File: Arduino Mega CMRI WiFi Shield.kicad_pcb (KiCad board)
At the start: 2 copper layers, 100 x 56 mm, 37 parts, among them IC2 VoltageRegulator-5V-3V3-TH, J1 Socket-2x4-TH, J10 Header-1x4-TH, J11 Header-1x4-TH, J12 Header-1x4-TH, J13 Header-1x4-TH, J14 Header-1x4-TH, J15 Header-1x4-TH, J16 Header-1x4-TH, J17 Header-1x4-TH, J18 Header-1x3-TH, J2 Header-1x4-TH, J3 Header-1x4-TH, J4 Header-1x4-TH, J5 Header-1x4-TH, J6 Header-1x4-TH, J7 Header-1x4-TH, J8 Header-1x4-TH, J9 Header-1x4-TH, Q1 Transistor-FET-.2A-2.6V-TH, Q2 Transistor-FET-.2A-2.6V-TH, Q3 Transistor-FET-.2A-2.6V-TH

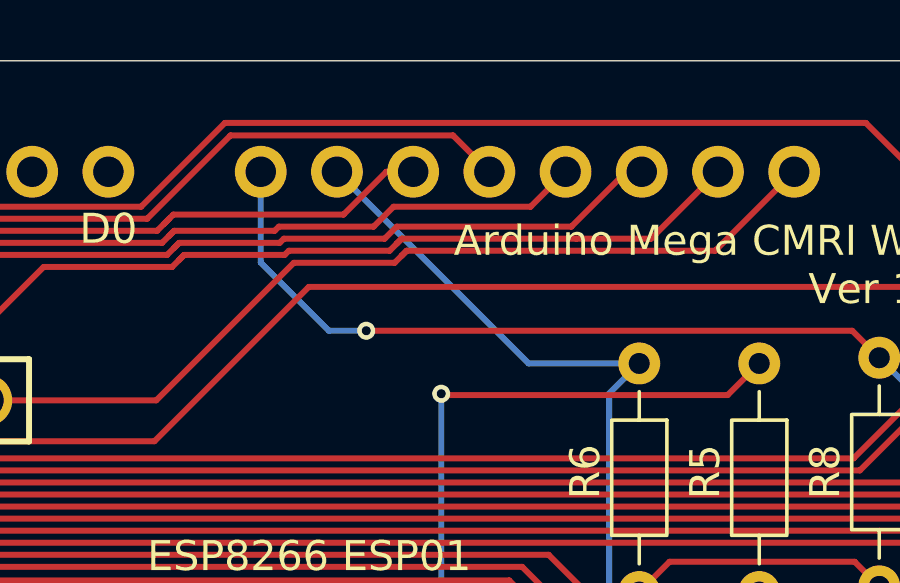
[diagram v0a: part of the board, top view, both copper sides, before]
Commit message: Swapped the RX and TX pins between the arduino and the ESP8266-ESP01 that was discovered on prototype board v1.2
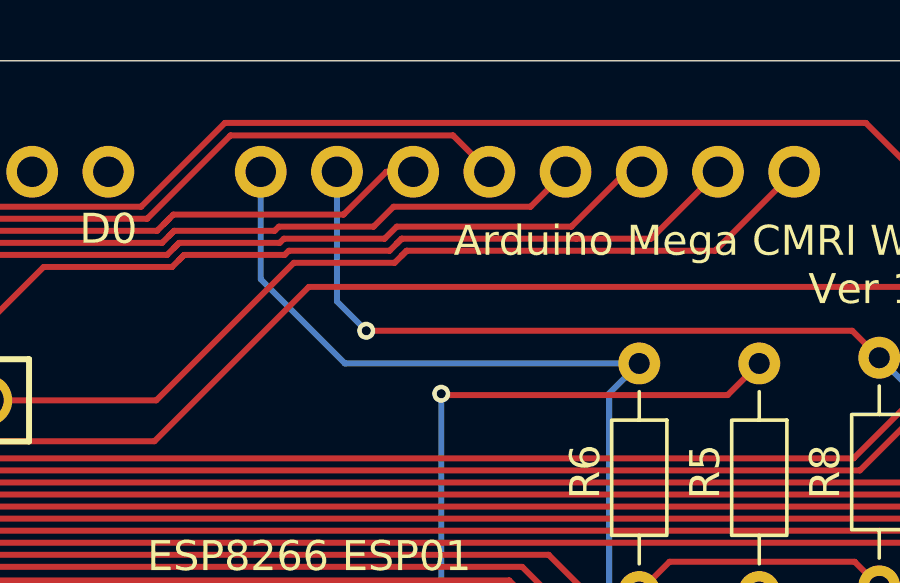
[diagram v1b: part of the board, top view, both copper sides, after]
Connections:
- A1 pad D14: /ESP8266ESP01WiFi/TX -> /ESP8266ESP01WiFi/RX
- A1 pad D15: /ESP8266ESP01WiFi/RX -> /ESP8266ESP01WiFi/TX
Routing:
- net /ESP8266ESP01WiFi/RX: track 39.2 -> 43.8 mm
- net /ESP8266ESP01WiFi/TX: track 50.8 -> 49.0 mm
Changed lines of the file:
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@@
 			)
 		)
-		(property "Datasheet" ""
+		(property "Datasheet" "https://www.mouser.com/datasheet/3/508/1/YAGEO_CFR_DATASHEET.pdf"
 			(at 0 0 270)
 			(layer "F.Fab")
@@
 			)
 		)
-		(property "Description" ""
+		(property "Description" "Resistor - 10K- 1/4W - 5% - Through Hole"
 			(at 0 0 270)
 			(layer "F.Fab")
@@
 			)
 		)
-		(property "Datasheet" ""
+		(property "Datasheet" "https://www.mouser.com/datasheet/3/508/1/YAGEO_CFR_DATASHEET.pdf"
 			(at 0 0 270)
 			(layer "F.Fab")
@@
 			)
 		)
-		(property "Description" ""
+		(property "Description" "Resistor - 10K- 1/4W - 5% - Through Hole"
 			(at 0 0 270)
 			(layer "F.Fab")
@@
 			(layers "*.Cu" "*.Mask")
 			(remove_unused_layers no)
-			(net 62 "/ESP8266ESP01WiFi/TX")
+			(net 71 "/ESP8266ESP01WiFi/RX")
 			(pinfunction "D14/TX3")
 			(pintype "bidirectional")
@@
 			(layers "*.Cu" "*.Mask")
 			(remove_unused_layers no)
-			(net 71 "/ESP8266ESP01WiFi/RX")
+			(net 62 "/ESP8266ESP01WiFi/TX")
 			(pinfunction "D15/RX3")
 			(pintype "bidirectional")
@@
 			)
 		)
-		(property "Datasheet" ""
+		(property "Datasheet" "https://www.mouser.com/datasheet/3/508/1/YAGEO_CFR_DATASHEET.pdf"
 			(at 0 0 270)
 			(layer "F.Fab")
@@
 			)
 		)
-		(property "Description" ""
+		(property "Description" "Resistor - 10K- 1/4W - 5% - Through Hole"
 			(at 0 0 270)
 			(layer "F.Fab")
@@
 			)
 		)
-		(property "Datasheet" ""
+		(property "Datasheet" "https://www.mouser.com/datasheet/3/508/1/YAGEO_CFR_DATASHEET.pdf"
 			(at 0 0 270)
 			(layer "F.Fab")
@@
 			)
 		)
-		(property "Description" ""
+		(property "Description" "Resistor - 10K- 1/4W - 5% - Through Hole"
 			(at 0 0 270)
 			(layer "F.Fab")
@@
 			)
 		)
-		(property "Datasheet" ""
+		(property "Datasheet" "https://www.mouser.com/datasheet/3/508/1/YAGEO_CFR_DATASHEET.pdf"
 			(at 0 0 270)
 			(layer "F.Fab")
@@
 			)
 		)
-		(property "Description" ""
+		(property "Description" "Resistor - 10K- 1/4W - 5% - Through Hole"
 			(at 0 0 270)
 			(layer "F.Fab")
@@
 			)
 		)
-		(property "Datasheet" ""
+		(property "Datasheet" "https://www.mouser.com/datasheet/3/508/1/YAGEO_CFR_DATASHEET.pdf"
 			(at 0 0 270)
 			(layer "F.Fab")
@@
 			)
 		)
-		(property "Description" ""
+		(property "Description" "Resistor - 10K- 1/4W - 5% - Through Hole"
 			(at 0 0 270)
 			(layer "F.Fab")
@@
 	)
 	(segment
-		(start 154.9 56.1)
-		(end 153.6572 56.1)
+		(start 172 57)
+		(end 173.004 58.004)
 		(width 0.2)
 		(layer "B.Cu")
@@
 	)
 	(segment
-		(start 172 57)
-		(end 173.004 58.004)
+		(start 153.924 55.124)
+		(end 153.924 50.8)
 		(width 0.2)
 		(layer "B.Cu")
@@
 	)
 	(segment
-		(start 151.384 53.8268)
-		(end 151.384 50.8)
+		(start 154.9 56.1)
+		(end 153.924 55.124)
 		(width 0.2)
 		(layer "B.Cu")
@@
 	)
 	(segment
-		(start 153.6572 56.1)
-		(end 151.384 53.8268)
-		(width 0.2)
-		(layer "B.Cu")
-		(net 62)
-	)
-	(segment
 		(start 152.0143 53.1704)
 		(end 148.6633 53.1704)
@@
 	)
 	(segment
-		(start 160.314 57.19)
-		(end 164 57.19)
+		(start 164 57.19)
+		(end 154.19 57.19)
 		(width 0.2)
 		(layer "B.Cu")
@@
 	)
 	(segment
+		(start 154.19 57.19)
+		(end 151.384 54.384)
+		(width 0.2)
+		(layer "B.Cu")
+		(net 71)
+	)
+	(segment
 		(start 165.0465 71.4631)
 		(end 162.9972 69.4138)
@@
 	)
 	(segment
-		(start 162.9972 58.1928)
-		(end 164 57.19)
+		(start 151.384 54.384)
+		(end 151.384 50.8)
 		(width 0.2)
 		(layer "B.Cu")
@@
 	)
 	(segment
-		(start 153.924 50.8)
-		(end 160.314 57.19)
+		(start 162.9972 58.1928)
+		(end 164 57.19)
 		(width 0.2)
 		(layer "B.Cu")

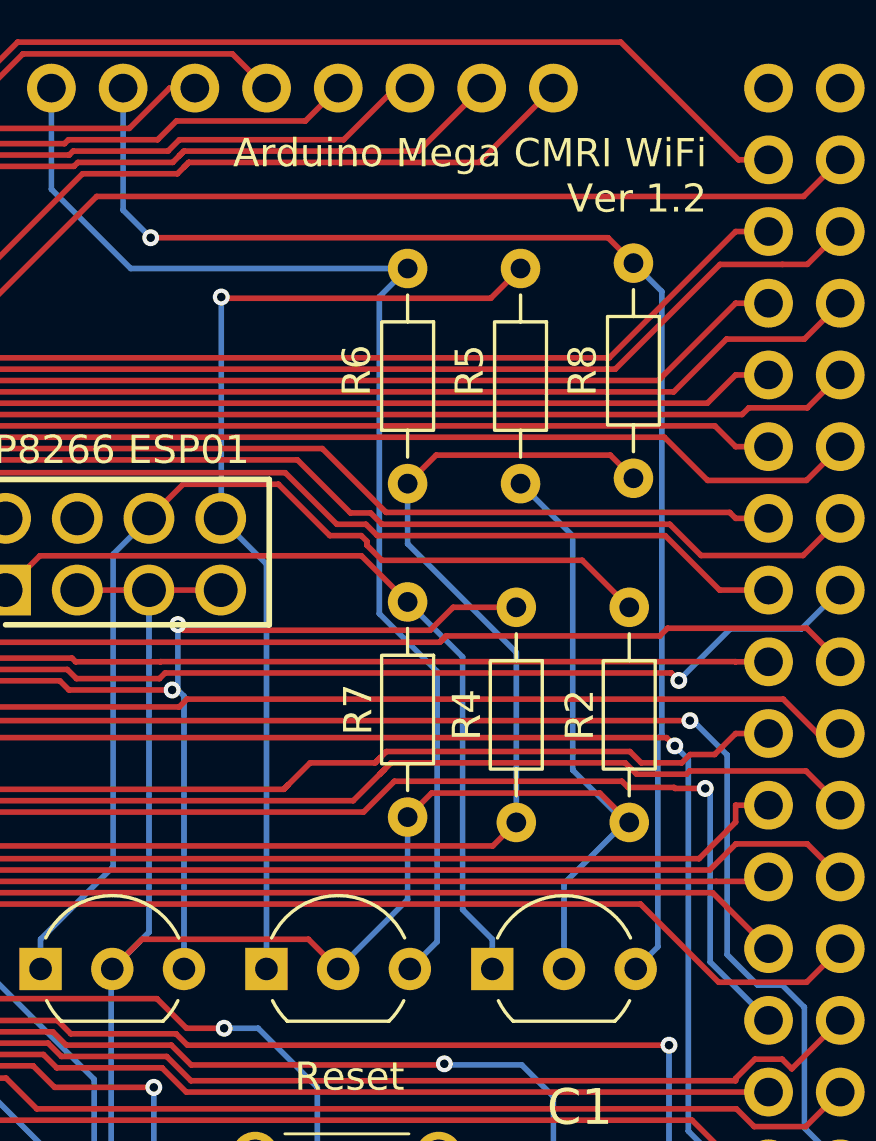
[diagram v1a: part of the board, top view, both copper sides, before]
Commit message: Updated version to 1.3 to reduce confusion from issue where Rx and TX needed swapped.
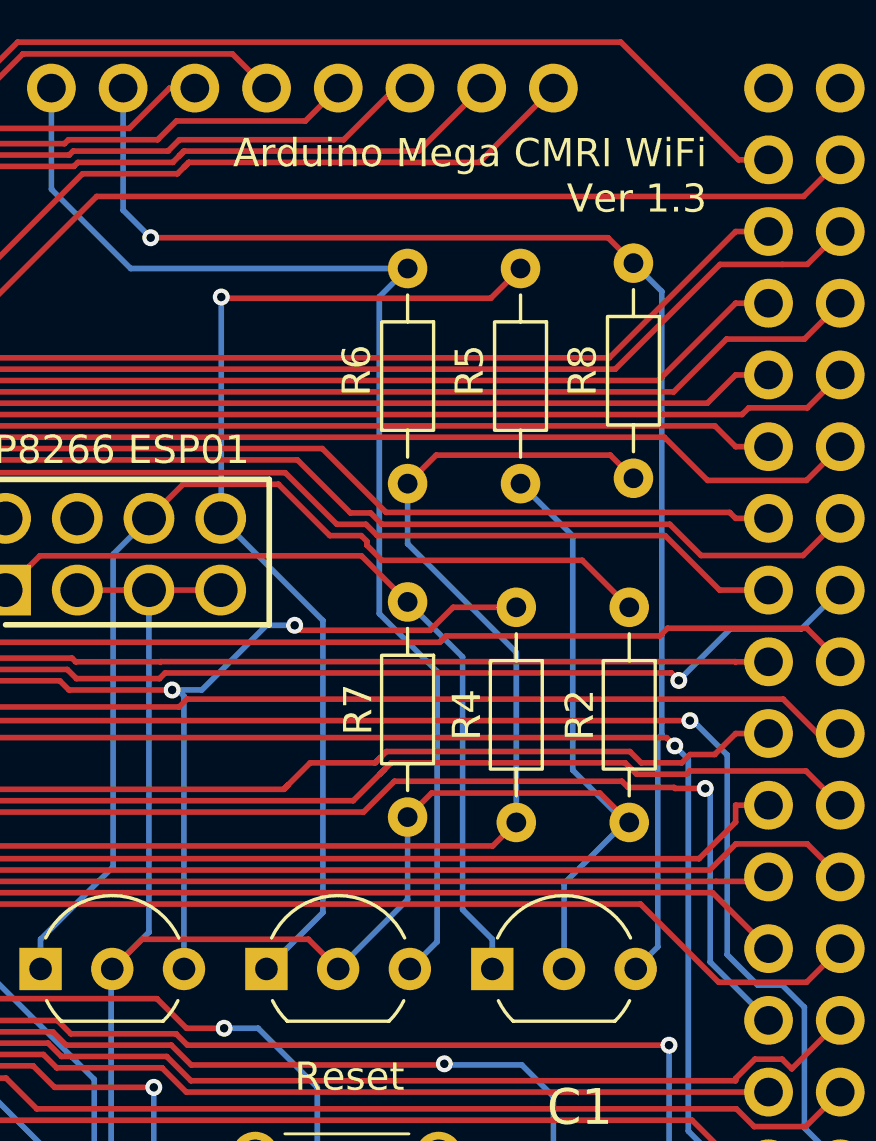
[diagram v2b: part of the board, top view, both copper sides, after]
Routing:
- net /ESP8266ESP01WiFi/LogicLevelShifter2/LOW: track 35.5 -> 37.2 mm
- net /ESP8266ESP01WiFi/Connected: track 86.9 -> 85.5 mm
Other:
- board text added: "Arduino Mega CMRI WiFi Ver 1.3"
- board text removed: "Arduino Mega CMRI WiFi Ver 1.2"
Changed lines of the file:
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@@
 		)
 	)
-	(gr_text "Arduino Mega CMRI WiFi\nVer 1.2"
+	(gr_text "Arduino Mega CMRI WiFi\nVer 1.3"
 		(at 174.6 55.3 0)
 		(layer "F.SilkS")
@@
 	)
 	(segment
-		(start 167.85 69.19)
+		(start 164.8001 70.0026)
 		(end 165.6127 69.19)
 		(width 0.2)
@@
 	)
 	(segment
-		(start 165.6127 69.19)
-		(end 164.8001 70.0026)
+		(start 139.0406 69.1841)
+		(end 114.1261 69.1841)
 		(width 0.2)
 		(layer "F.Cu")
@@
 	)
 	(segment
-		(start 139.0406 69.1841)
-		(end 114.1261 69.1841)
+		(start 165.6127 69.19)
+		(end 167.85 69.19)
 		(width 0.2)
 		(layer "F.Cu")
@@
 	)
 	(segment
-		(start 151.681 71.7931)
-		(end 143.9287 71.7931)
+		(start 160 69.8278)
+		(end 160.1748 70.0026)
 		(width 0.2)
 		(layer "F.Cu")
@@
 	)
 	(segment
-		(start 156.0657 70.0026)
-		(end 155.8631 69.8)
+		(start 151.681 71.7931)
+		(end 143.9287 71.7931)
 		(width 0.2)
 		(layer "F.Cu")
@@
 	)
 	(segment
-		(start 164.8001 70.0026)
-		(end 156.0657 70.0026)
+		(start 160.1748 70.0026)
+		(end 164.8001 70.0026)
 		(width 0.2)
 		(layer "F.Cu")
@@
 	)
 	(via
-		(at 155.8631 69.8)
+		(at 160 69.8278)
 		(size 0.6)
 		(drill 0.3)
@@
 	)
 	(segment
+		(start 160 69.8278)
+		(end 159 69.8278)
+		(width 0.2)
+		(layer "B.Cu")
+		(net 47)
+	)
+	(segment
 		(start 113.1348 53.1305)
 		(end 114.3 51.9653)
@@
 	)
 	(segment
+		(start 156.7098 72.118)
+		(end 155.8631 72.118)
+		(width 0.2)
+		(layer "B.Cu")
+		(net 47)
+	)
+	(segment
+		(start 159 69.8278)
+		(end 156.7098 72.118)
+		(width 0.2)
+		(layer "B.Cu")
+		(net 47)
+	)
+	(segment
 		(start 113.1348 68.1928)
 		(end 113.1348 53.1305)
@@
 	(segment
 		(start 155.8631 72.118)
-		(end 155.8631 69.8)
-		(width 0.2)
-		(layer "B.Cu")
-		(net 47)
-	)
-	(segment
-		(start 155.8631 72.118)
 		(end 155.6608 72.118)
 		(width 0.2)
@@
 	)
 	(segment
+		(start 161 80)
+		(end 159 82)
+		(width 0.2)
+		(layer "B.Cu")
+		(net 88)
+	)
+	(segment
 		(start 157.4 66.02)
 		(end 157.38 66.04)
@@
 	(segment
 		(start 157.38 66.04)
-		(end 159 67.66)
+		(end 161 69.66)
 		(width 0.2)
 		(layer "B.Cu")
@@
 	)
 	(segment
-		(start 159 67.66)
-		(end 159 82)
+		(start 157.4 58.2)
+		(end 157.4 66.02)
 		(width 0.2)
 		(layer "B.Cu")
@@
 	)
 	(segment
-		(start 157.4 58.2)
-		(end 157.4 66.02)
+		(start 161 69.66)
+		(end 161 80)
 		(width 0.2)
 		(layer "B.Cu")
